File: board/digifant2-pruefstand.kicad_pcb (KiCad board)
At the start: 2 copper layers, 144 x 169 mm, 60 parts, among them J0 VW ECU HARNESS, J1 12V BENCH IN, J2 IDLE VALVE N71, J3 OLED / UI I2C, Q1 2N7002, Q2 P-MOS -30V >=5A, Q3 2N7002, Q5 2N7002, SW1 PUSH, SW2 PUSH, SW3 PUSH, U1 INA226 (0x40), U2 MCP4728 (0x60), U3 INA226 (0x41), U4 AD9833, U5 Raspberry Pi Pico, U6 TS5A3159A, U7 TS5A3159A, U8 TS5A3159A, Y1 25MHz

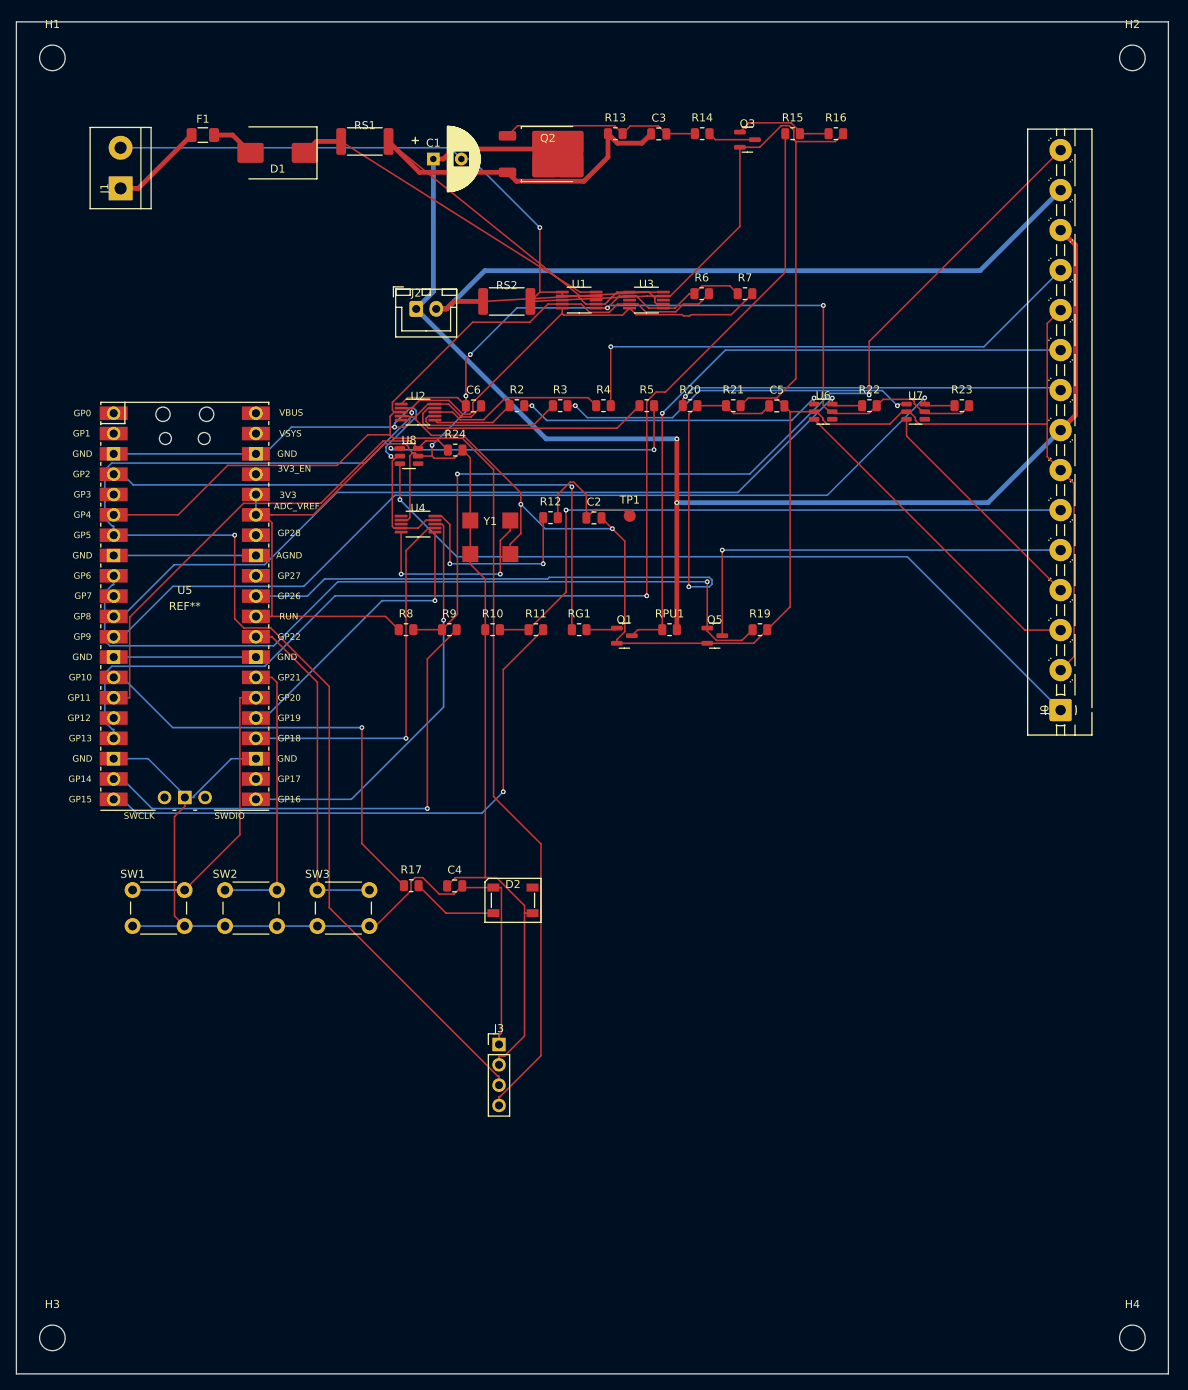
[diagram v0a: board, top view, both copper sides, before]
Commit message: Hand-route the U1/U3/RS1/RS2 pocket + add GND pour: DRC clean
User fixed the remaining Kelvin-sense-trace violations (2 shorting_items,
2 clearance, 5 tracks_crossing) by hand in KiCad's interactive router,
and added a B.Cu GND pour, which also picked up the 3 previously-
unconnected GND pads near the Pico (U5) for free.

DRC is now clean: 0 unconnected items, 0 shorts, 0 clearance/crossing
violations. One minor starved_thermal note remains (U5 GND pad 42 has
1 pour spoke instead of the zone's preferred 2 -- connected fine, just
a slightly weaker thermal/mechanical joint). Everything else is the
same pre-existing cosmetic noise (silkscreen, lib_footprint_mismatch).

Co-Authored-By: Claude Sonnet 5 <noreply@anthropic.com>
Claude-Session: https://claude.ai/code/session_01GgbvgUaRvNV7WyBdaSUkDT
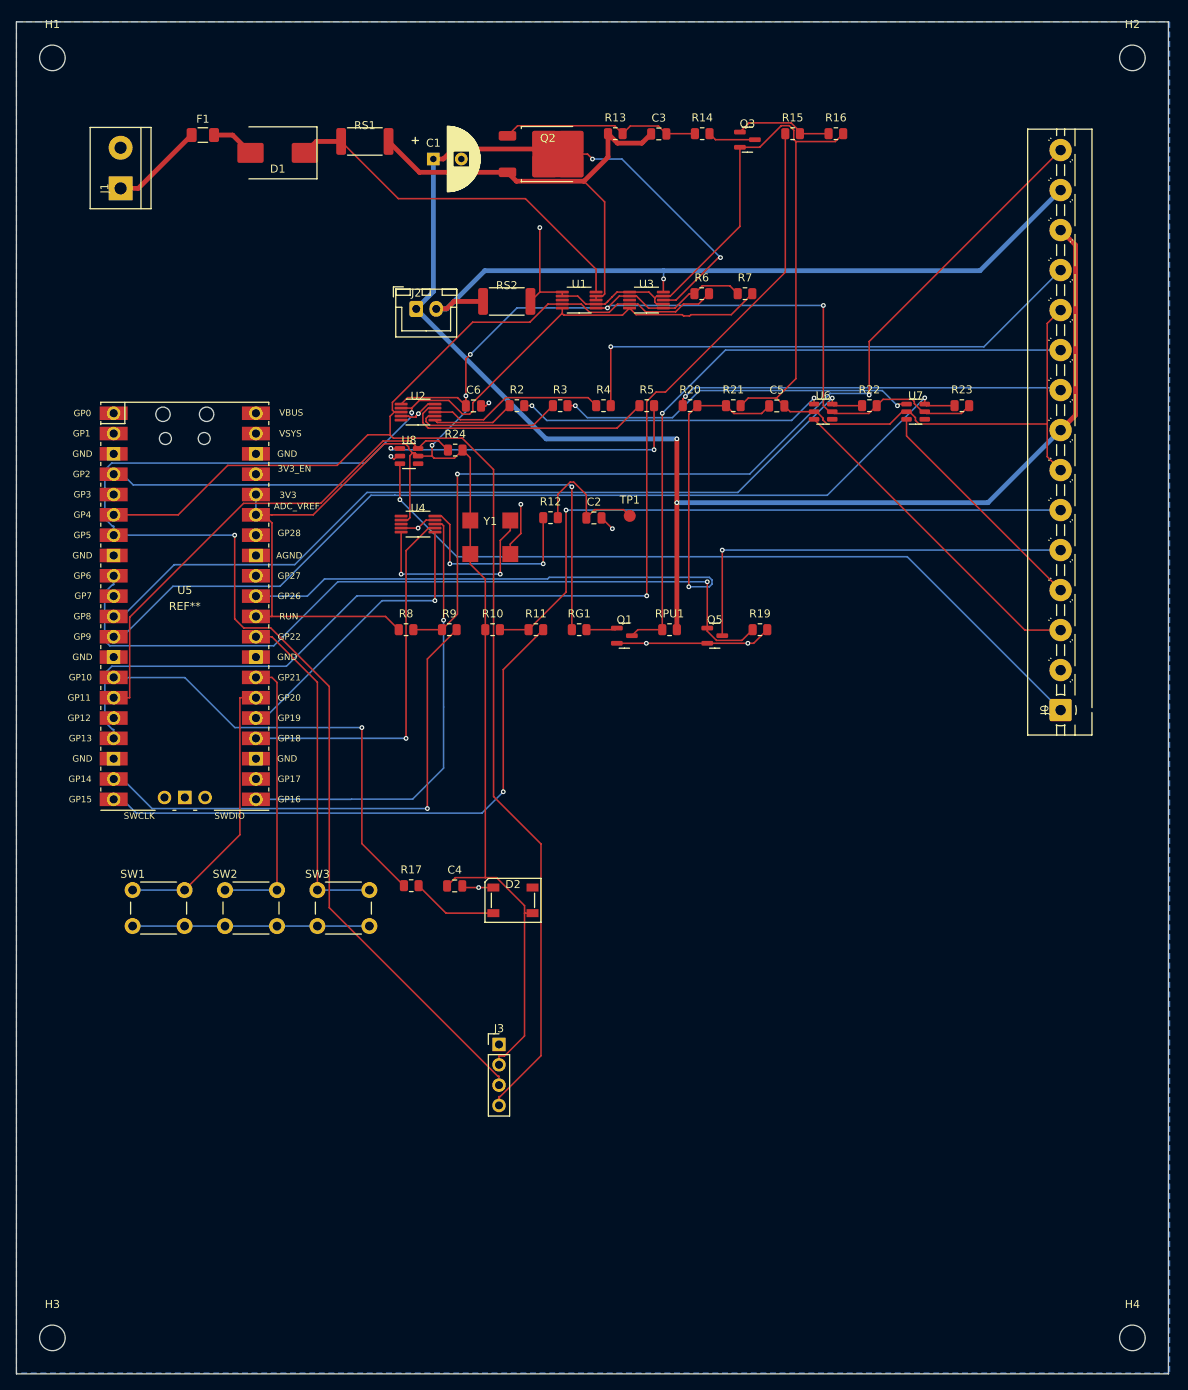
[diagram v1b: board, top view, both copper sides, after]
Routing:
- net GND: track 590.8 -> 237.9 mm, vias 5 -> 10
- net +12V_ECU_SW: track 185.6 -> 220.6 mm, vias 2 -> 4
- net VW_PIN23_VALVE_RETURN: track 113.0 -> 93.1 mm, vias 0 -> 1
- net +12V_ECU: track 72.8 -> 56.9 mm
- net GP16_SPI_CS: track 52.1 -> 56.5 mm
- net +12V_POST_D1: track 42.4 -> 46.5 mm
- added copper zone on B.Cu, net GND

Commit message: Add missing AD9833 decoupling caps (C7, C8) before fab
The layout review flagged AD9833's COMP/CAP_2V5 pins as decoupling-only
with no cap ever added -- a real gap, not cosmetic, since skipping it
would mean a bodge-wire fix after fab. Added per ADI's recommended
application circuit: 100nF from each pin to AGND.

- digifant2_pruefstand.py: C7 (COMP) and C8 (CAP_2V5), both to gnd.
- Schematic: regenerated a scratch copy to get circuit-synth's correct
  net/label placement math, then spliced just the new symbol + label
  blocks into the committed schematic (preserving all prior manual
  work). Removed the two now-stale no_connect flags on U4's COMP/
  CAP_2V5 pins. Renamed the auto-generated net labels from circuit-
  synth's "N$4"/"N$5" to "U4_COMP"/"U4_CAP2V5" -- the board already had
  an unrelated net named "N$4" elsewhere, which collided.
- PCB: placed both caps by hand next to U4, in the same tightly-packed
  corner as the U1/U3/RS1/RS2 pocket. Both hot-side traces are routed
  and DRC-clean. C8's GND pad has one short unrouted line left -- this
  corner fights scripted routing exactly like that other pocket did,
  so it's left for the same quick manual finish in KiCad rather than
  more trial-and-error coordinate math.

Co-Authored-By: Claude Sonnet 5 <noreply@anthropic.com>
Claude-Session: https://claude.ai/code/session_01GgbvgUaRvNV7WyBdaSUkDT
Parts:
- added C7: 100nF, Capacitor_SMD:C_0805_2012Metric, F.Cu at (44.0, 61.8)
- added C8: 100nF, Capacitor_SMD:C_0805_2012Metric, F.Cu at (39.0, 62.8)
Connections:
- U4 pad 1: unconnected-(U4-Pad1-Pad1) -> U4_COMP
- U4 pad 3: unconnected-(U4-Pad3-Pad3) -> U4_CAP2V5
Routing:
- net U4_CAP2V5: track 0.00 -> 8.14 mm
- net U4_COMP: track 0.00 -> 3.14 mm

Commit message: Fix VW-17 divider headroom before fab: R20 15k -> 20k
Found in USE_CASES.md's verification pass: the divider's stated 9V
worst case (VW-17, airflow-pot reference) divided down to 3.6V through
the old 15k/10k ratio -- right at the RP2040 ADC's absolute-max input
rating, zero margin. Nominal 5V operation was always safe; it was
specifically that stated fault/worst-case voltage with no headroom.

R20 -> 20k changes the ratio from 10/25=0.4 to 10/30=0.333, so the same
9V worst case now lands at 3.0V (0.6V of real margin) while nominal 5V
still sits mid-range at 1.67V. Value-only change (same footprint, no
topology change), so no re-routing needed -- updated in the circuit
source, schematic, and PCB.

Co-Authored-By: Claude Sonnet 5 <noreply@anthropic.com>
Claude-Session: https://claude.ai/code/session_01XcEuUwwCT37oProAm8HYeY
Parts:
- R20: value 15k -> 20k
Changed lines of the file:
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@@
 			)
 		)
-		(property "Value" "15k"
+		(property "Value" "20k"
 			(at 0 2 0)
 			(layer "F.Fab")

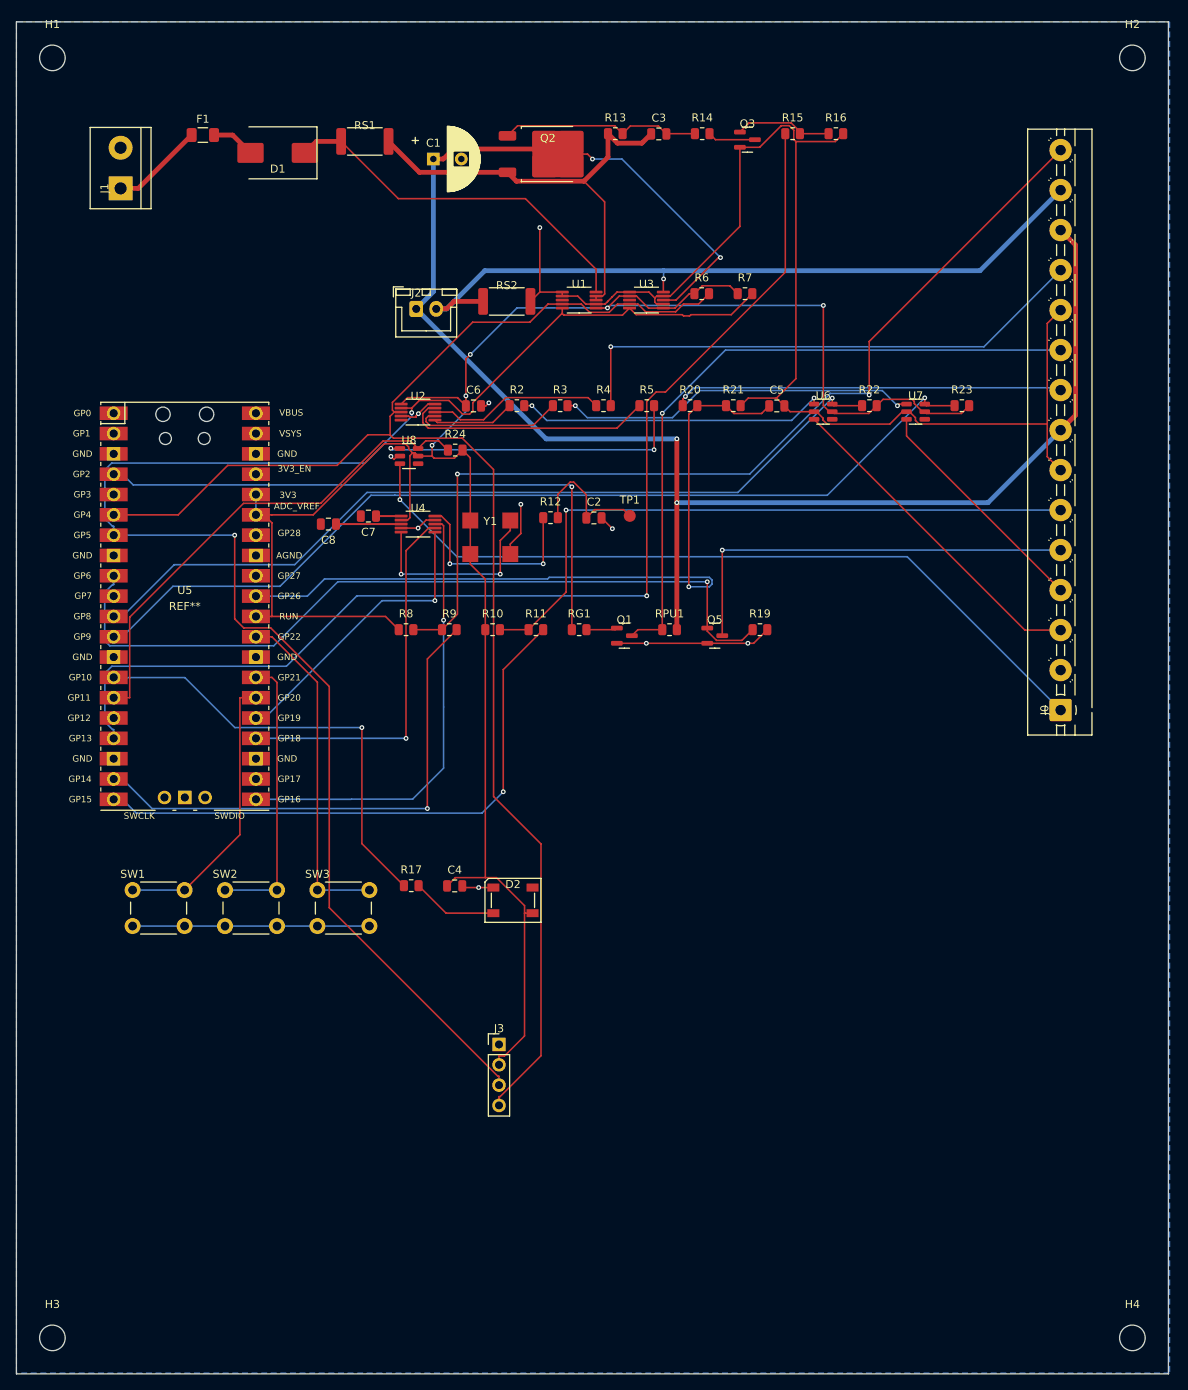
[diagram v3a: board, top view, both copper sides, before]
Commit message: Fix RS2's parallel ground path and give the knock output a real path out
Two of the three genuinely-open findings from USE_CASES.md:

1. RS2 (idle-valve shunt) sat as a separate tap to GND, in parallel with
   the ECU's own low-side driver on VW-23 -- both reached the same shared
   GND, so return current split between RS2 and the ECU's internal switch,
   and U3 only ever measured whatever fraction happened through RS2.
   Understated the true current, worst exactly when the ECU driver was on.
   Fixed: RS2 is now truly in series (valve -> RS2 -> VW-23), so 100% of
   the return current crosses it. U3's IN+/IN- assignment was swapped
   (IN+ keeps the net that already had a routed path to J0, IN- takes the
   new sense-side net) purely to minimize how much existing routing needed
   to change -- sign of the current reading is a firmware convention
   either way.

2. AD9833 knock output dead-ended at a single test pad with no path out.
   J0 is already full (15/15 positions; VW-4/5/7 were never broken out
   there), so this needed a separate small tap, same idea as J2 for the
   idle valve. A proper 2-pin JST connector was tried first (matching
   J2's style) but every placement attempt shorted a different existing
   net -- this corner of the board is threaded with +12V_ECU_SW,
   VW_PIN10/11/12, and GP8/GP9/GP13/GP26 on both layers. Used two small
   bare test pads (TP1 signal, TP2 ground, same footprint as the original
   TP1) instead, which fit where the connector wouldn't.

Both required real topology changes, not just added parts -- updated the
circuit source AND spliced the corresponding net-label renames into the
committed schematic (not just the PCB), otherwise a future PCB-from-
schematic sync would have silently reverted the RS2 fix.

One new residual, same class as the existing U1/U3/RS1/RS2 pocket: U3
pin 9's own local GND-mesh neighbours and its new sense-net connection
both need to route through the same tight spot. Tried by hand and via
Freerouting f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
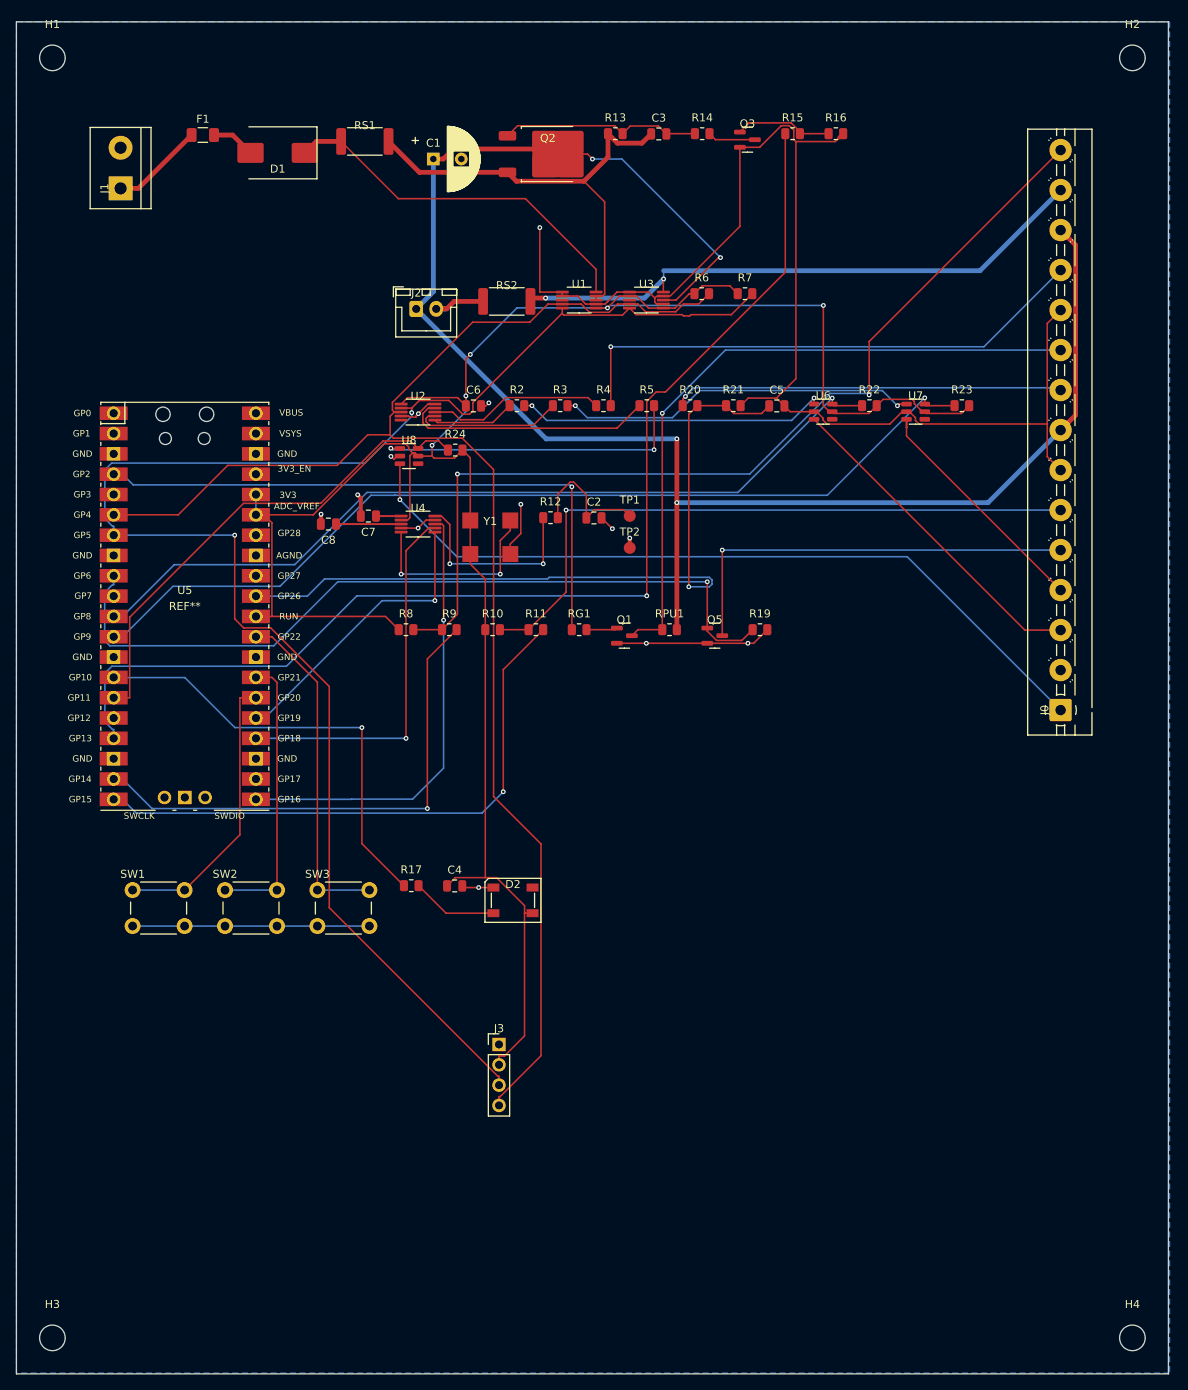
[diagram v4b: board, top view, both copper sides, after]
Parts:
- added TP2: KNOCK GND (to VW-5), TestPoint:TestPoint_Pad_D1.5mm, F.Cu at (76.7, 65.8)
- TP1: value KNOCK OUT -> KNOCK OUT (to VW-4)
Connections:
- J2 pad 2: VW_PIN23_VALVE_RETURN -> VALVE_RETURN_SENSE
- RS2 pad 1: VW_PIN23_VALVE_RETURN -> VALVE_RETURN_SENSE
- RS2 pad 2: GND -> VW_PIN23_VALVE_RETURN
- U3 pad 9: GND -> VALVE_RETURN_SENSE
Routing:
- net VW_PIN23_VALVE_RETURN: track 93.1 -> 74.3 mm, vias 1 -> 2
- net VALVE_RETURN_SENSE: track 0.00 -> 7.54 mm
- net GND: track 237.9 -> 240.6 mm, vias 10 -> 13
- net VW_PIN10: track 29.3 -> 30.4 mm
